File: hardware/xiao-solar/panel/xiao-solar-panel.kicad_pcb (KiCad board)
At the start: 2 copper layers, 96 x 81.5 mm, 155 parts, among them J1 SOLAR, J2 VIN2 5-20V, J3 NTC 10k (103AT), J4 BATTERY, J5 I2C rail, Q2 AO3400A (ship FET), Q3 HJ8205, U1 BQ25798RQMR, U2 DW01A, U3 XIAO nRF52840, U4 Wio-SX1262 for XIAO, U5 SHT40-AD1B, U7 INA219AIDCNR

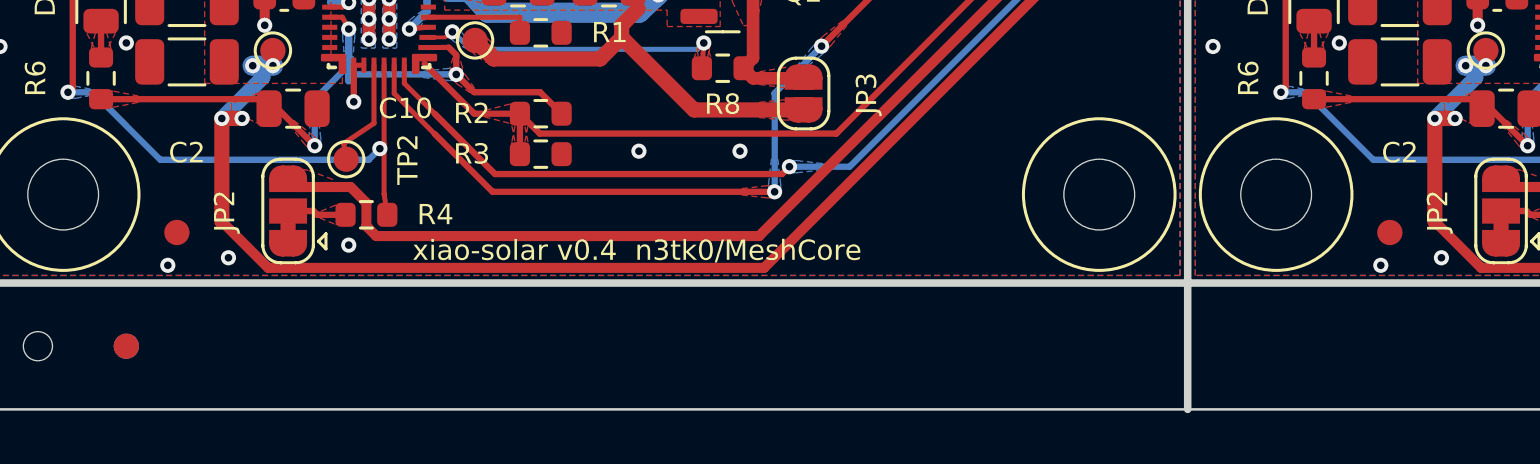
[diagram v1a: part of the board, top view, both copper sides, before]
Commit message: hardware: fiducial clearance 0.65 mm so the GND pour stays under mask (JLC DFM), move one GND via
Co-Authored-By: Claude Opus 5.5 <noreply@anthropic.com>
Claude-Session: https://claude.ai/code/session_01P5Km81NY9NPL6RpKFGVEbH
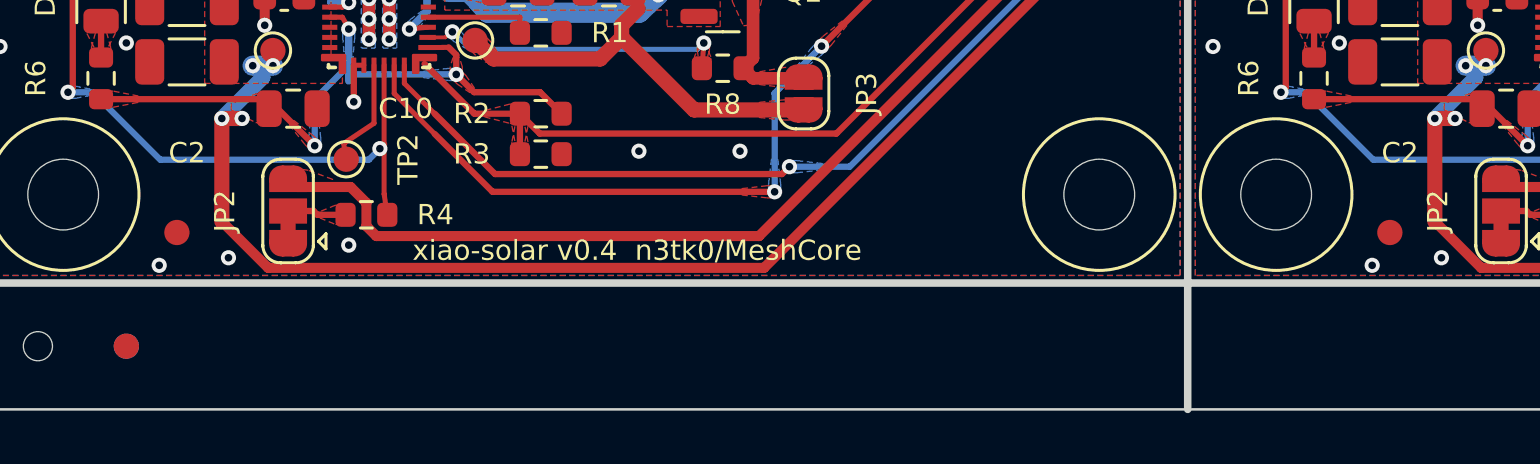
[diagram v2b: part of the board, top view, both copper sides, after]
